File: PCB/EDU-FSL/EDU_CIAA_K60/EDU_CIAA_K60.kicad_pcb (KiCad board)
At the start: 2 copper layers, 85.8 x 137 mm, 188 parts, among them J1 USB OTG, J2 TB_1X2, J3 JTAG DEBUG USB, J4 JTAG DIRECTO, J5 RS485, P1 CONN_20X2, P2 CONN_20X2, Q1 2N7002, Q2 2N7002, Q3 2N7002, Q4 2N7002, Q5 2N7002, Q6 2N7002, T1 SRF2012, T2 SRF2012, U1 MIC2025-2YM, U10 MK60FX512VLQ15, U11 SI501, U2 PRTR5V0U2X, U3 NCP1117ST33T3G, U4 SI501, U5 FT2232H, U6 74HC244, U7 PRTR5V0U2X, U8 93C56, U9 SP1486EEN-L, Y1 32.768KHZ

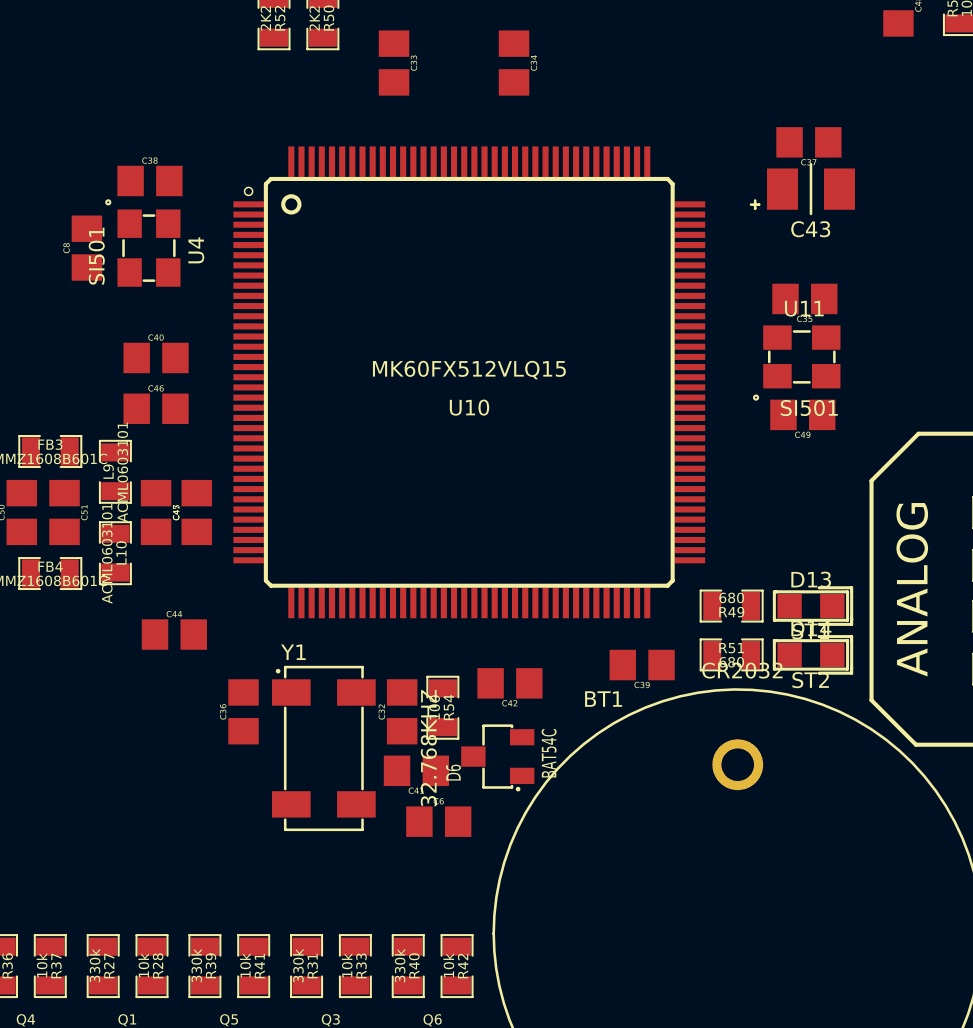
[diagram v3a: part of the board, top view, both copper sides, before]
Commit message: Se actualizaron los numeros de parte de todos los inductores
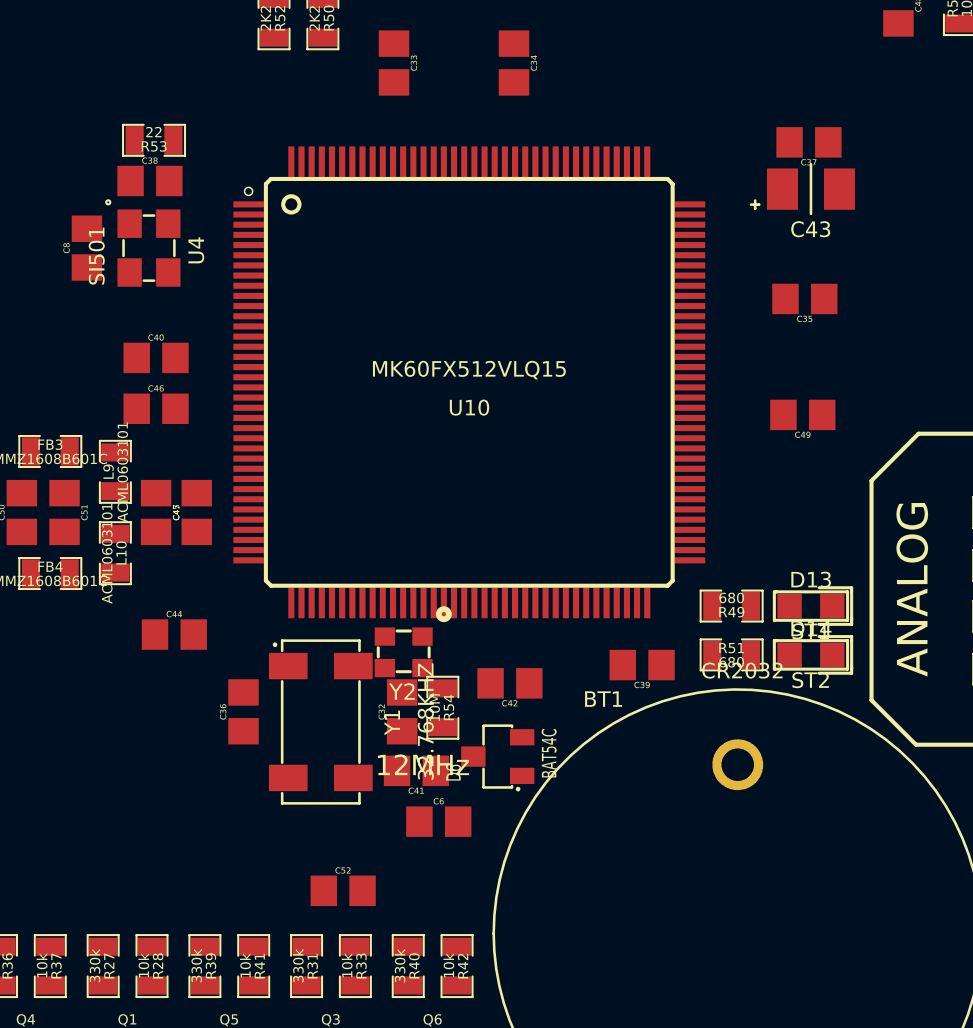
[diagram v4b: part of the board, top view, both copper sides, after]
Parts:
- removed U11: SI501, SI501_C
- added C52: 18pF, c_0805, F.Cu at (221.8, 167.0)
- added R53: 22, r_0805, F.Cu at (212.5, 130.1)
- added Y2: 12MHz, FA238V-XTAL, F.Cu at (225.7, 154.5)
- C49: value 100nF -> 18pF
- R54: value 100 -> 10M
- moved Y1 1.31 mm to (220.7, 158.7)
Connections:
- C49 pad 1: +3.3V -> N-00000114
- R54 pad 1: N-0000087 -> N-00000114
- R54 pad 2: N-00000135 (its old number) -> N-00000101
- U10 pad 3: /GPIO/GPIO6 -> N-00000130
- U10 pad 45: N-0000087 -> N-00000101
- U10 pad 46: (no net) -> N-00000114
- U10 pad 55: (no net) -> /GPIO/GPIO8
- U10 pad 60: /CPU/TEC_F0 -> (no net)
- U10 pad 61: /CPU/TEC_F1 -> (no net)
- U10 pad 62: /CPU/TEC_F2 -> (no net)
- U10 pad 63: /CPU/TEC_F3 -> (no net)
- U10 pad 73: (no net) -> /GPIO/GPIO7
- U10 pad 77: /GPIO/ADC0_1 -> (no net)
- U10 pad 78: /GPIO/ADC0_2 -> /GPIO/ADC0_1
- U10 pad 79: /GPIO/ADC0_3 -> /GPIO/ADC0_2
- U10 pad 80: (no net) -> /GPIO/ADC0_3
- U10 pad 83: (no net) -> /CPU/TEC_F0
- U10 pad 84: (no net) -> /CPU/TEC_F1
- U10 pad 85: (no net) -> /CPU/TEC_F2
- U10 pad 86: (no net) -> /CPU/TEC_F3
- U10 pad 89: /GPIO/GPIO7 -> (no net)
- U10 pad 90: /GPIO/GPIO8 -> (no net)

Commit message: Limpieza de archivos innecesarios PCB V0.0
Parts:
- moved R53 112.4 mm to (286.1, 215.0), turned to 270 degrees
- moved Y2 81.1 mm to (285.5, 209.3), turned to 270 degrees
- moved C52 74.2 mm to (278.5, 214.9)
- moved U4 50.4 mm to (222.1, 86.0)
- moved C8 50.4 mm to (218.9, 86.0)
- moved FB3 46.8 mm to (252.3, 158.4)
- moved FB4 45.0 mm to (252.1, 146.1)
- moved D14 43.7 mm to (207.7, 132.4), turned to 180 degrees
- moved D13 43.5 mm to (207.7, 130.2), turned to 180 degrees
- moved C43 41.9 mm to (202.9, 131.2), turned to 270 degrees
- moved R10 41.0 mm to (222.1, 82.2)
- moved R52 40.8 mm to (244.7, 155.2), turned to 90 degrees
- moved R50 40.6 mm to (246.8, 155.2), turned to 90 degrees
- moved C50 40.4 mm to (238.4, 124.2), turned to 225 degrees
- moved U8 39.4 mm to (230.4, 80.4)
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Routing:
- net GND: track 152.2 -> 1287.0 mm, vias 0 -> 34
- net +3.3V: track 0.00 -> 742.0 mm, vias 0 -> 17
- net +5V: track 50.8 -> 474.4 mm, vias 0 -> 5
- net /CPU/PULS_3: track 0.00 -> 110.5 mm
- net /CPU/PULS_2: track 0.00 -> 99.3 mm
- net /Fuente/USB_VBUS: track 0.00 -> 96.4 mm, vias 0 -> 4
- net /CPU/TEC_F2: track 0.00 -> 93.5 mm, vias 0 -> 4
- net N-00000135: track 0.00 -> 93.3 mm, vias 0 -> 3
- net /CPU/USB_ID: track 0.00 -> 91.8 mm, vias 0 -> 2
- net /CPU/TEC_F1: track 0.00 -> 89.5 mm, vias 0 -> 4
- net /CPU/PULS_1: track 0.00 -> 89.2 mm
- net /CPU/TEC_F3: track 0.00 -> 88.4 mm, vias 0 -> 4
- net /CPU/USB_DP: track 0.00 -> 86.8 mm, vias 0 -> 2
- net /CPU/USB_DM: track 0.00 -> 86.4 mm, vias 0 -> 2
- net /GPIO/GPIO5: track 0.00 -> 85.5 mm, vias 0 -> 1
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- added copper zone on B.Cu, net /JTAG/CHS_DBG
- added copper zone on F.Cu, net /JTAG/CHS_DBG
- added copper zone on B.Cu, net /USB OTG/CHS_OTG
- added copper zone on F.Cu, net /USB OTG/CHS_OTG
- added copper zone on B.Cu, net GND
- added copper zone on F.Cu, net GND
- added copper zone on B.Cu, net GNDA
- added copper zone on F.Cu, net GNDA

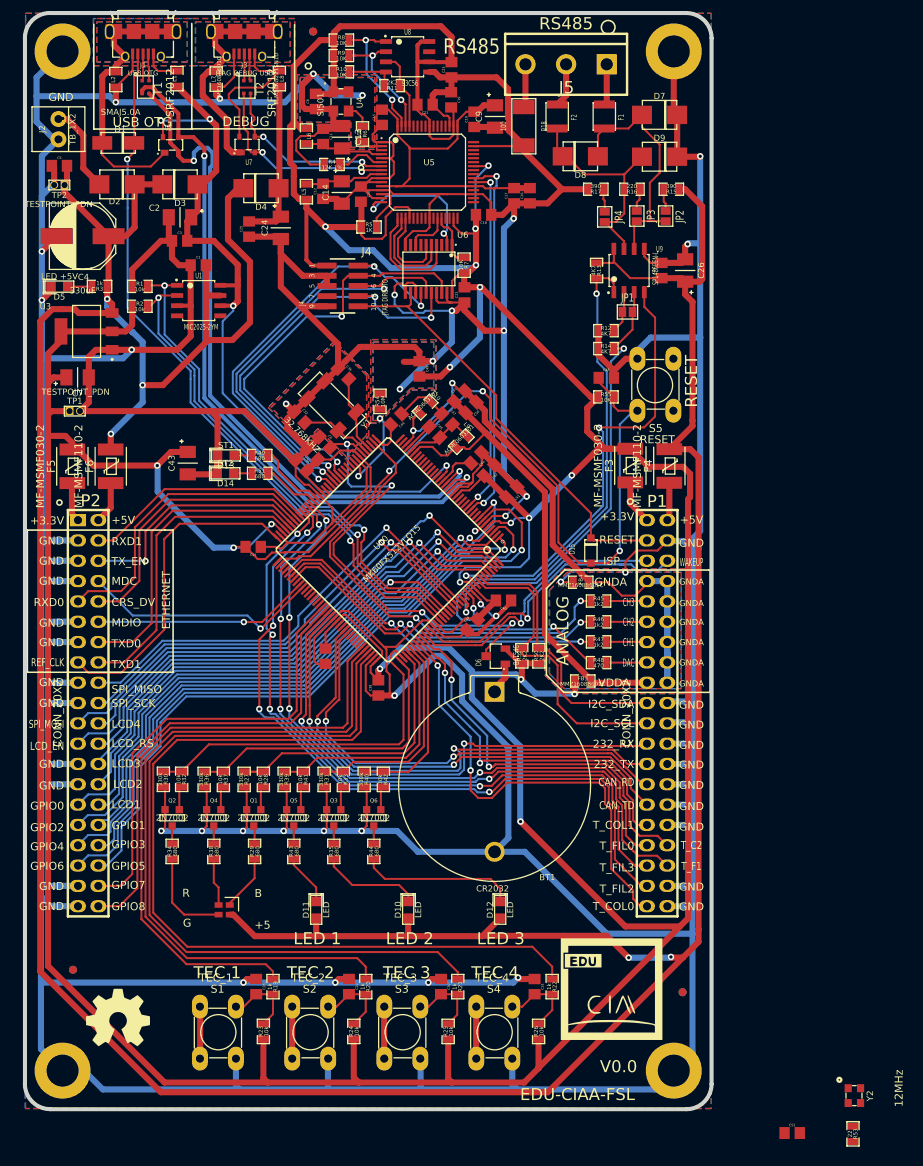
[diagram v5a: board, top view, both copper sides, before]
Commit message: Modificados los pines de las teclas
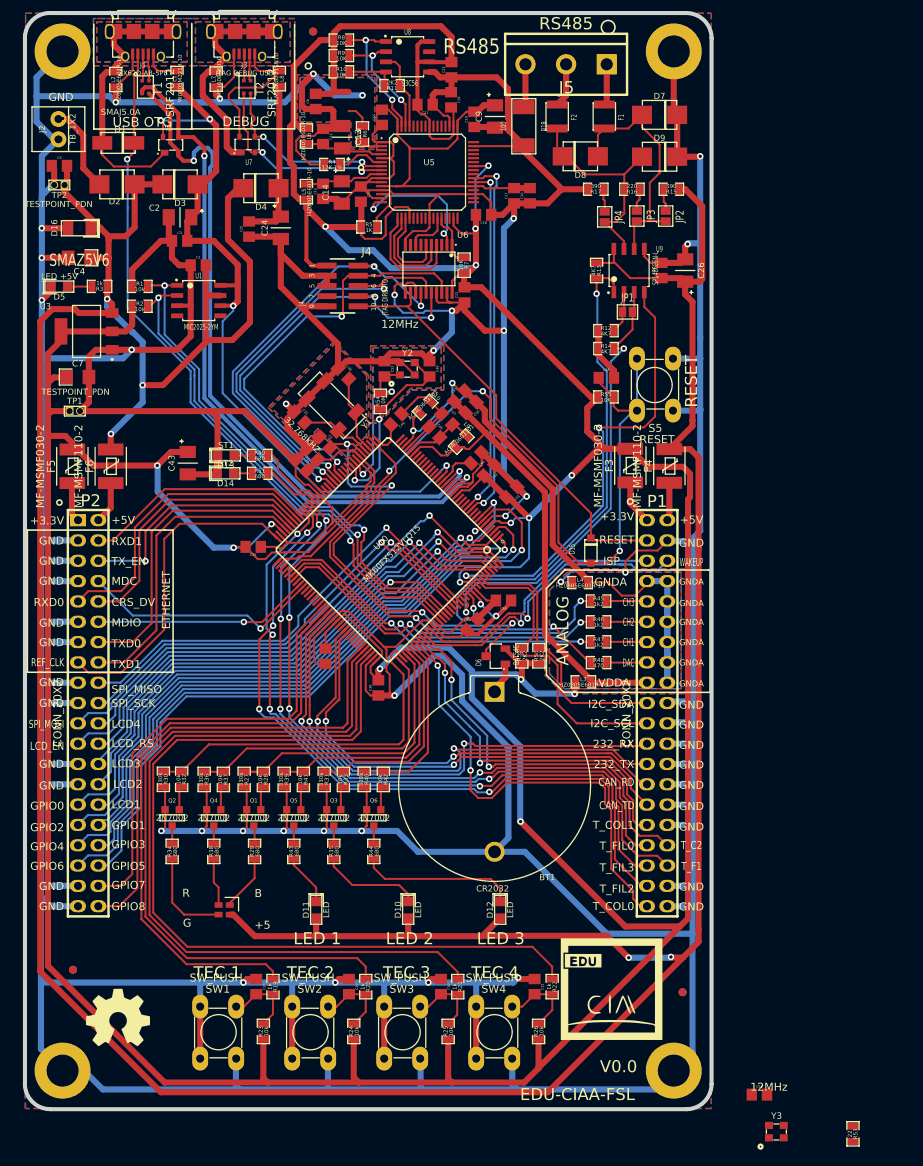
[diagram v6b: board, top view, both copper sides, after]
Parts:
- removed FB3, FB4: MMZ1608B601C, SM0805
- removed S1: TEC_1, PUSH_SWITCH_THT
- removed S2: TEC_2, PUSH_SWITCH_THT
- removed S3: TEC_3, PUSH_SWITCH_THT
- removed S4: TEC_4, PUSH_SWITCH_THT
- removed U4: SI501, SI501_C
- added C53: 27pF, c_0805, F.Cu at (274.4, 210.1)
- added D16: SMAZ5V6, SOD123F, F.Cu at (189.4, 101.8)
- added L3: HZ0805E601R-10, SM0805, F.Cu at (252.4, 158.5)
- added L4: HZ0805E601R-10, SM0805, F.Cu at (252.0, 146.1)
- added SW1: SW_PUSH, PUSH_SWITCH_THT, F.Cu at (204.5, 199.1)
- added SW2: SW_PUSH, PUSH_SWITCH_THT, F.Cu at (216.0, 199.1)
- added SW3: SW_PUSH, PUSH_SWITCH_THT, F.Cu at (227.5, 199.1)
- added SW4: SW_PUSH, PUSH_SWITCH_THT, F.Cu at (239.0, 199.1)
- added Y3: 12MHz, FA238V-XTAL, F.Cu at (275.6, 215.5)
- C4: value 330uF -> 10uF; footprint c_elec_8x10 -> c_1206_tantalio
- C49, C52: value 18pF -> 27pF
- C7: footprint c_1206POL -> c_1206_tantalio
- C8: value 100nF -> 27pF
- J1: value USB OTG -> ZX62D-AB-5P8
- L1: value ~ -> MI0805M221R-10
- L2, L5, L6: value ~ -> HZ0805E601R-10
- R6: value 100 -> 10M
- moved C52 108.3 mm to (227.5, 119.4), turned to 270 degrees
- moved Y2 105.3 mm to (229.5, 120.1), turned to 0 degrees
- moved C4 2.73 mm to (189.4, 105.5)
- moved C49 1.27 mm to (233.2, 119.4)
- moved S5 0.05 mm to (263.6, 124.6)
- moved C7 0.05 mm to (189.2, 120.4)
- moved R54 0.05 mm to (227.0, 123.4)
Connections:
- C8 pad 1: +3.3V -> N-00000204
- R6 pad 1: N-00000207 -> N-00000204
- R6 pad 2: N-00000171 (its old number) -> N-00000169
- S5 pad 2: GND -> N-00000135
- S5 pad 3: (no net) -> GND
- S5 pad 4: (no net) -> GND
- U5 pad 2: N-00000171 (its old number) -> N-00000204
- U5 pad 3: (no net) -> N-00000169
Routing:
- net (no net): track 26.0 -> 0.00 mm
- net N-00000129: track 2.68 -> 24.0 mm, vias 0 -> 2
- net GND: track 1287.0 -> 1304.5 mm
- net +3.3V: track 742.0 -> 727.0 mm, vias 17 -> 15
- net N-00000128: track 11.0 -> 20.9 mm
- net N-00000204: track 0.00 -> 7.14 mm
- net N-00000135: track 93.3 -> 99.7 mm
- net N-00000226: track 9.52 -> 13.4 mm
- net N-00000228: track 9.66 -> 13.5 mm
- net +5V: track 474.4 -> 477.8 mm
- net N-00000211: track 9.46 -> 12.8 mm
- net N-00000227: track 10.0 -> 13.3 mm
- net N-00000207: track 3.17 -> 0.00 mm
- net N-00000171 (its old number): track 2.74 -> 0.00 mm
- net N-00000169: track 0.00 -> 0.72 mm
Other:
- net class Alimentación: trace_width 0.254 -> 0.762

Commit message: V1.2
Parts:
- moved Y3 140.1 mm to (220.7, 86.6)
- moved C53 136.3 mm to (218.6, 85.8), turned to 90 degrees
- moved R53 85.4 mm to (243.9, 140.8)
- moved C8 5.59 mm to (224.5, 85.8)
- moved D13 5.05 mm to (203.3, 127.8)
- moved D14 4.86 mm to (203.3, 130.3)
- moved C43 4.73 mm to (198.7, 129.1)
- moved R49 4.61 mm to (207.9, 128.0)
- moved R51 4.55 mm to (207.9, 130.3)
- moved C35 2.52 mm to (211.5, 144.1), turned to 90 degrees
- moved U2 1.57 mm to (202.4, 91.4), turned to 90 degrees
- moved R10 0.46 mm to (222.1, 81.8)
- moved C40 0.40 mm to (242.1, 148.6)
- moved R9 0.30 mm to (222.1, 79.9)
- moved R8 0.25 mm to (222.1, 78.0)
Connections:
- U10 pad 83: /CPU/TEC_F0 -> /CPU/TEC_F2
- U10 pad 84: /CPU/TEC_F1 -> /CPU/TEC_F3
- U10 pad 85: /CPU/TEC_F2 -> /CPU/TEC_F1
- U10 pad 86: /CPU/TEC_F3 -> /CPU/TEC_F0
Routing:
- net GND: track 1304.5 -> 1508.1 mm, vias 34 -> 49
- net /GPIO/ADC0_3: track 1.26 -> 45.0 mm, vias 0 -> 2
- net /GPIO/ADC0_1: track 82.1 -> 42.5 mm, vias 3 -> 2
- net /CPU/TEC_F2: track 93.5 -> 74.3 mm, vias 4 -> 1
- net /CPU/TEC_F0: track 85.2 -> 68.7 mm, vias 4 -> 1
- net /CPU/TEC_F3: track 88.4 -> 72.0 mm, vias 4 -> 1
- net /CPU/TEC_F1: track 89.5 -> 73.2 mm, vias 4 -> 1
- net /GPIO/GPIO8: track 59.2 -> 73.6 mm, vias 0 -> 1
- net N-00000169: track 0.72 -> 13.1 mm
- net /GPIO/ENET_REF_CLK: track 40.5 -> 32.9 mm
- net /GPIO/ENET_TXD1: track 38.6 -> 31.2 mm
- net /GPIO/ENET_RXD1: track 29.2 -> 36.0 mm
- net /GPIO/ENET_TXD0: track 38.1 -> 31.5 mm
- net /USB OTG/CHS_OTG: track 34.3 -> 40.7 mm
- net /Fuente/USB_VBUS: track 96.4 -> 101.7 mm
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
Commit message: EDU-CIAA-FSL V0.0 actualización del PCB
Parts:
- added TP3: ~, 4mm, F.Cu at (264.6, 197.5)
- C13, C14, C24, C9: value 4,7uF -> 10uF
- C32, C36: value 18pF -> 20pF
- C49, C52, C53, C8: value 27pF -> 20pF
- D2, D3, D4: value MBRS130LT3G -> PMEG3020EH
- D5: value LED +5V -> LED red
- D7, D8, D9: value P6SMB12CAT3G -> PSD12C
- J2: value TB_1X2 -> 5Vcc Input
- J3: value JTAG DEBUG USB -> ZX62D-AB-5P8
- J5: value RS485 -> TB_1X3
- JP1, JP2, JP3, JP4: value JUMPER -> JUMPER-2
- L10, L9: value ACML0603101 -> MI0805M221R-10
- L7: value MMZ1608B601C -> MI0805M221R-10
- L8: value BLM18KG221SN1D -> MI0805M221R-10
- SW1: value SW_PUSH -> TEC_1
- SW2: value SW_PUSH -> TEC_2
- SW3: value SW_PUSH -> TEC_3
- SW4: value SW_PUSH -> TEC_4
- T1, T2: value SRF2012 -> DLW21HN900SQ2
- U8: value 93C56 -> 93C46
- U9: value SP1486EEN-L -> SN65HVD1176DR
- moved D10 11.6 mm to (218.9, 187.1)
- moved D11 11.5 mm to (230.5, 187.0)
- moved FD3 4.00 mm to (264.8, 201.3)
- moved FD6 4.00 mm to (264.8, 201.3)
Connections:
- D10 pad 2: N-00000222 (its old number) -> N-00000211
- D11 pad 2: N-00000212 (its old number) -> N-00000223
- R35 pad 1: N-00000222 (its old number) -> N-00000223
- R43 pad 1: N-00000212 (its old number) -> N-00000211
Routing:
- net GND: track 1508.1 -> 1476.6 mm, vias 49 -> 47
- net N-00000223: track 0.00 -> 12.6 mm
- net N-00000222 (its old number): track 12.6 -> 0.00 mm
- net N-00000212 (its old number): track 6.46 -> 0.00 mm
- net N-00000211: track 0.00 -> 6.46 mm
- net +5V: track 478.9 -> 479.7 mm
- net N-00000149: vias 1 -> 0
